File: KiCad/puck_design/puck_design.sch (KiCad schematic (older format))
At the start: 29 parts, among them J1 Coax_Jack, J2 SJ-2523-SMT-TR, Q1 CSD16406Q3, Q2 CSD16406Q3, U1 ITG-3701, U2 BT840F, U3 TE832-M1, U4 MCP73831-2, U5 BQ29700DSER

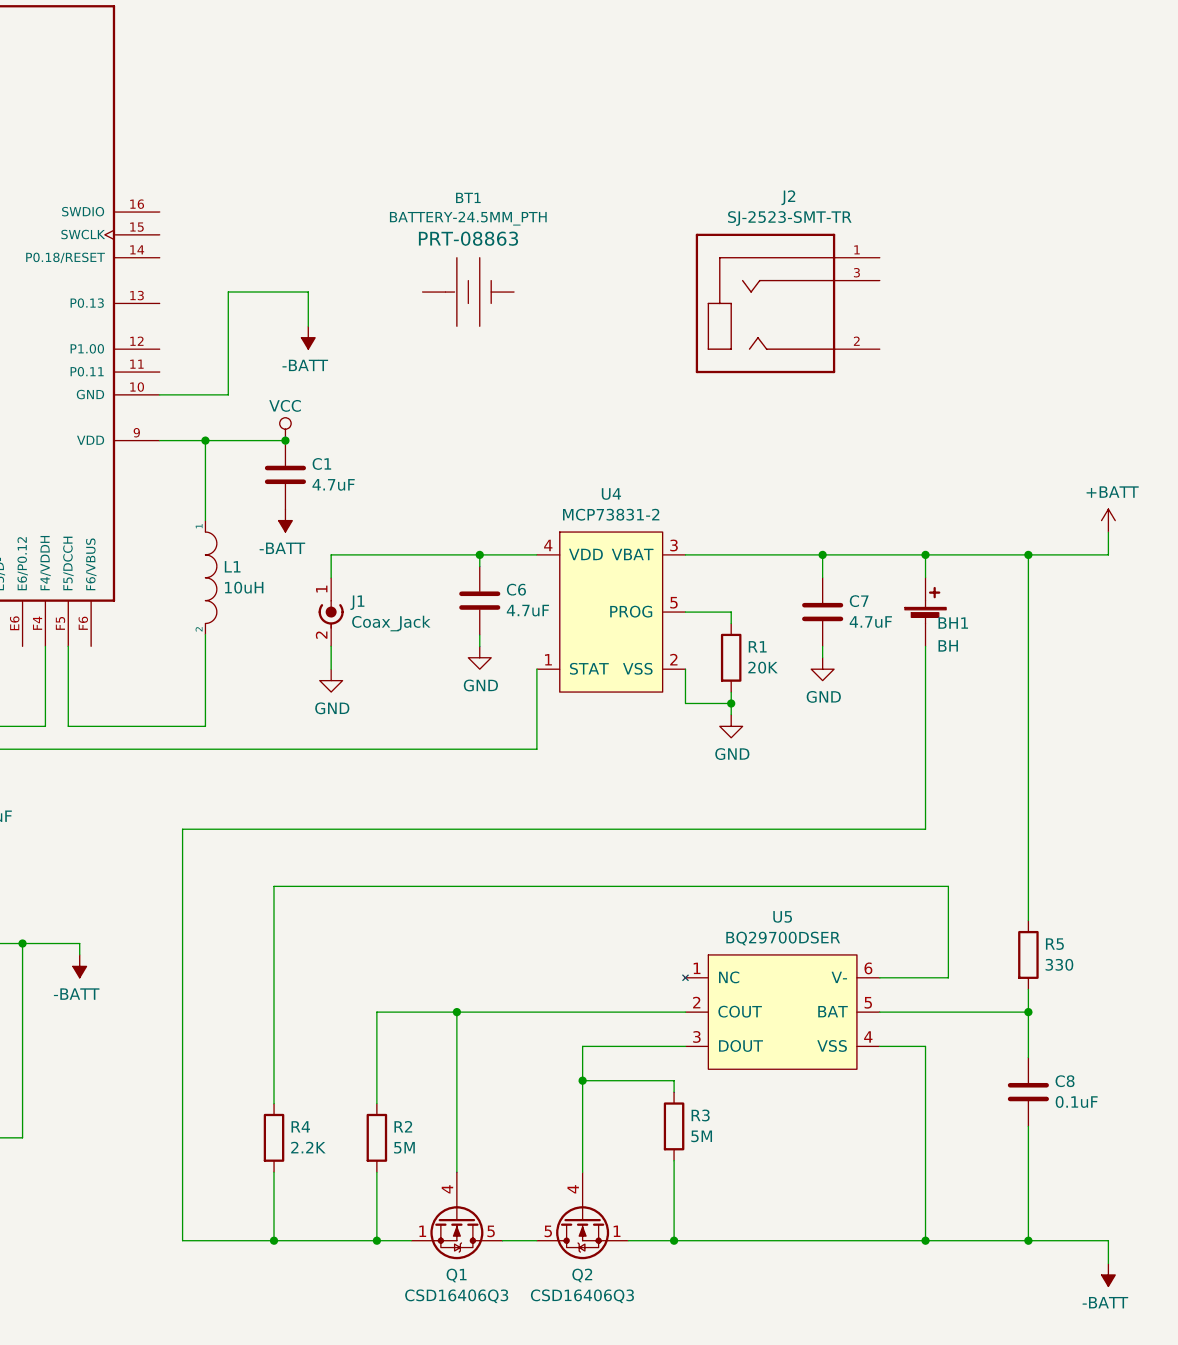
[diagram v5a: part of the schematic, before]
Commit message: Added inductor footprint
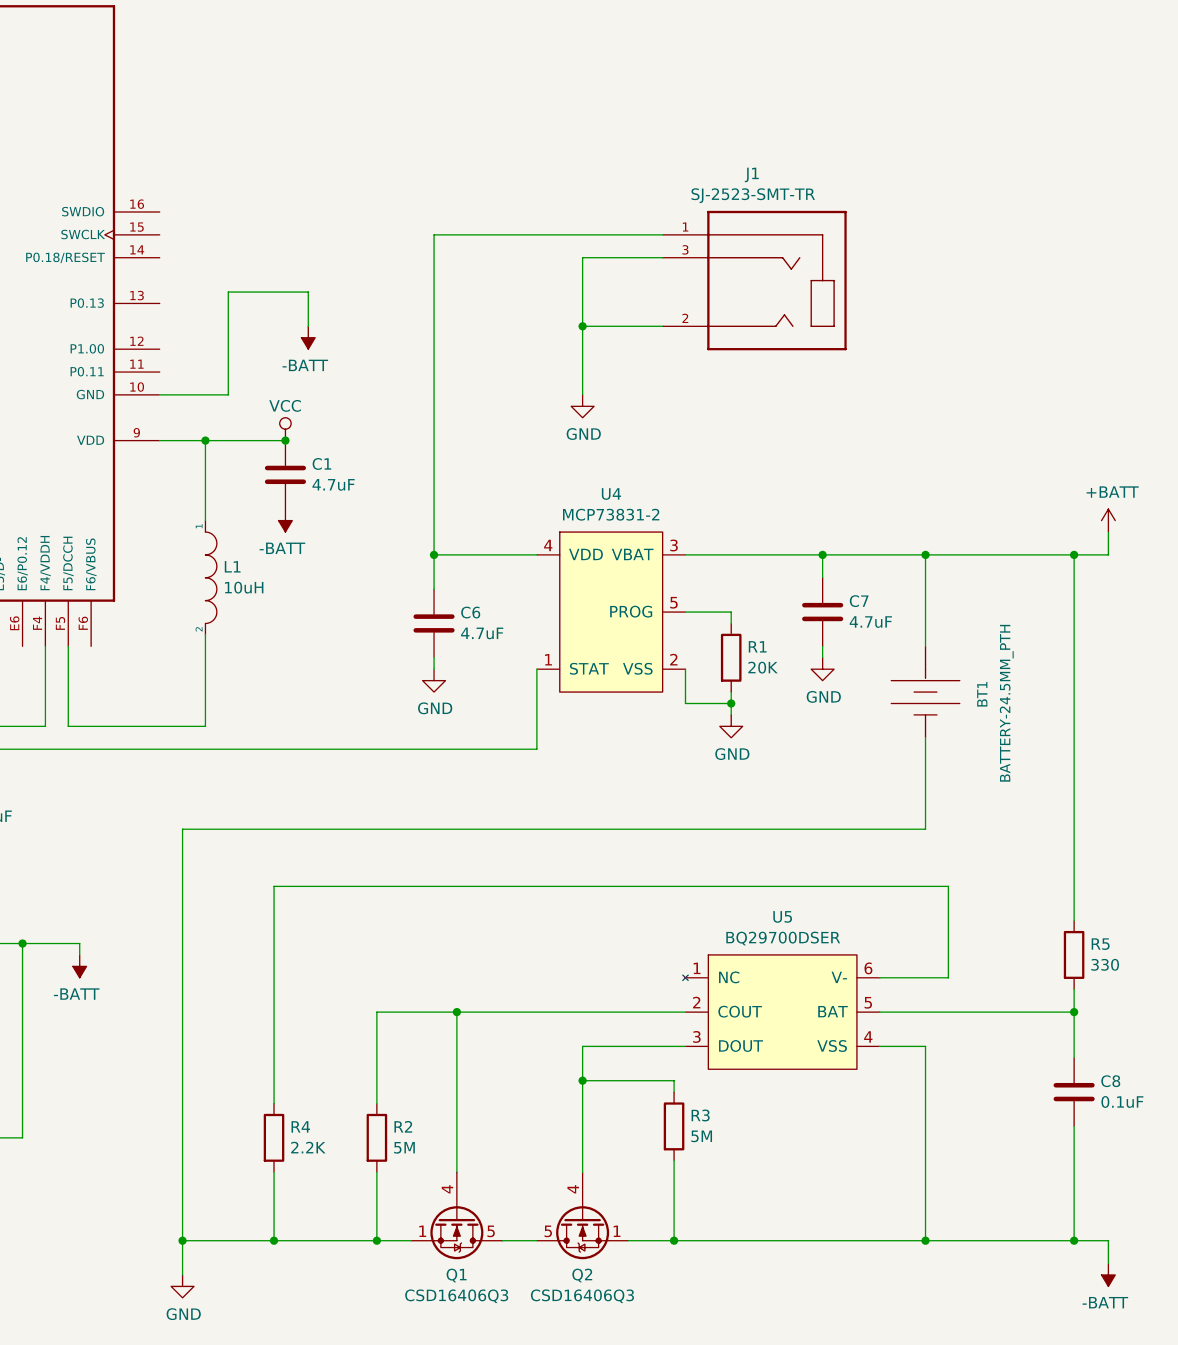
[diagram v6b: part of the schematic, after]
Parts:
- removed BH1: BH, puck_footprints:BATTCON_24.5MM_PTH, symbol Device:Battery_Cell
- removed J1: Coax_Jack, puck_footprints:CUI_SJ-2523-SMT-TR, symbol Connector:Conn_Coaxial_Power
- BT1: Field4 PRT-08863 -> (none)
- L1: footprint (none) -> puck_footprints:CAPC2012X135N
- renumbered J2 to J1
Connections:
- net +BATT: now also BT1.1 (+)
- net GND: now also BT1.2 (-), J1.2, J1.3, Q1.1 (S), Q1.2 (S), Q1.3 (S), R2.2, R4.2
- net at C6.1, U4.4 (VDD): now also J1.1
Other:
- moved on the sheet: C6, C8, J1, R5
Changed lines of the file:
@@
-$EndComp
-$Comp
-L Device:Battery_Cell BH1
-U 1 1 5C20407B
-P 10000 3450
-F 0 "BH1" H 10050 3450 50  0000 L CNN
-F 1 "BH" H 10050 3350 50  0000 L CNN
-F 2 "puck_footprints:BATTCON_24.5MM_PTH" V 10000 3510 50  0001 C CNN
-F 3 "~" V 10000 3510 50  0001 C CNN
-	1    10000 3450
-	1    0    0    -1
 $EndComp
 $Comp
@@
 L power:GND #PWR0115
 U 1 1 5C1E4D3E
-P 7400 3650
-F 0 "#PWR0115" H 7400 3400 50  0001 C CNN
-F 1 "GND" H 7405 3477 50  0000 C CNN
-F 2 "" H 7400 3650 50  0001 C CNN
-F 3 "" H 7400 3650 50  0001 C CNN
-	1    7400 3650
+P 8500 2450
+F 0 "#PWR0115" H 8500 2200 50  0001 C CNN
+F 1 "GND" H 8505 2277 50  0000 C CNN
+F 2 "" H 8500 2450 50  0001 C CNN
+F 3 "" H 8500 2450 50  0001 C CNN
+	1    8500 2450
 	1    0    0    -1
 $EndComp
@@
 L Device:C C6
 U 1 1 5C1C0D7E
-P 8050 3350
-F 0 "C6" H 8165 3396 50  0000 L CNN
-F 1 "4.7uF" H 8165 3305 50  0000 L CNN
-F 2 "puck_footprints:CAPC2012X140N" H 8088 3200 50  0001 C CNN
-F 3 "~" H 8050 3350 50  0001 C CNN
-	1    8050 3350
+P 7850 3450
+F 0 "C6" H 7965 3496 50  0000 L CNN
+F 1 "4.7uF" H 7965 3405 50  0000 L CNN
+F 2 "puck_footprints:CAPC2012X140N" H 7888 3300 50  0001 C CNN
+F 3 "~" H 7850 3450 50  0001 C CNN
+	1    7850 3450
 	1    0    0    -1
 $EndComp
@@
 L power:GND #PWR0119
 U 1 1 5C1CC93A
-P 8050 3550
-F 0 "#PWR0119" H 8050 3300 50  0001 C CNN
-F 1 "GND" H 8055 3377 50  0000 C CNN
-F 2 "" H 8050 3550 50  0001 C CNN
-F 3 "" H 8050 3550 50  0001 C CNN
-	1    8050 3550
+P 7850 3650
+F 0 "#PWR0119" H 7850 3400 50  0001 C CNN
+F 1 "GND" H 7855 3477 50  0000 C CNN
+F 2 "" H 7850 3650 50  0001 C CNN
+F 3 "" H 7850 3650 50  0001 C CNN
+	1    7850 3650
 	1    0    0    -1
 $EndComp
@@
 $EndComp
 Wire Wire Line
-	8050 3150 8050 3200
-Connection ~ 8050 3150
-Wire Wire Line
-	8050 3150 8300 3150
-Wire Wire Line
-	8050 3500 8050 3550
+	7850 3600 7850 3650
 Wire Wire Line
 	9550 3550 9550 3600
@@
 	9550 3150 10000 3150
 Connection ~ 9550 3150
-Wire Wire Line
-	10000 3150 10000 3250
 $Comp
 L puck_library:BQ29700DSER U5
@@
 L Device:R R5
 U 1 1 5C3A4125
-P 10450 4900
-F 0 "R5" H 10520 4946 50  0000 L CNN
-F 1 "330" H 10520 4855 50  0000 L CNN
-F 2 "puck_footprints:0805-NO" V 10380 4900 50  0001 C CNN
-F 3 "~" H 10450 4900 50  0001 C CNN
-	1    10450 4900
+P 10650 4900
+F 0 "R5" H 10720 4946 50  0000 L CNN
+F 1 "330" H 10720 4855 50  0000 L CNN
+F 2 "puck_footprints:0805-NO" V 10580 4900 50  0001 C CNN
+F 3 "~" H 10650 4900 50  0001 C CNN
+	1    10650 4900
 	1    0    0    -1
 $EndComp
@@
 L Device:C C8
 U 1 1 5C3A412C
-P 10450 5500
-F 0 "C8" H 10565 5546 50  0000 L CNN
-F 1 "0.1uF" H 10565 5455 50  0000 L CNN
-F 2 "puck_footprints:CAPC2012X140N" H 10488 5350 50  0001 C CNN
-F 3 "~" H 10450 5500 50  0001 C CNN
-	1    10450 5500
-	1    0    0    -1
-$EndComp
-Wire Wire Line
-	10450 5650 10450 6150
-Wire Wire Line
-	10450 5050 10450 5150
-Wire Wire Line
-	9800 5150 10450 5150
-Connection ~ 10450 5150
-Wire Wire Line
-	10450 5150 10450 5350
+P 10650 5500
+F 0 "C8" H 10765 5546 50  0000 L CNN
+F 1 "0.1uF" H 10765 5455 50  0000 L CNN
+F 2 "puck_footprints:CAPC2012X140N" H 10688 5350 50  0001 C CNN
+F 3 "~" H 10650 5500 50  0001 C CNN
+	1    10650 5500
+	1    0    0    -1
+$EndComp
+Wire Wire Line
+	10650 5650 10650 6150
+Wire Wire Line
+	10650 5050 10650 5150
+Connection ~ 10650 5150
+Wire Wire Line
+	10650 5150 10650 5350
 Wire Wire Line
 	8900 6150 10000 6150
@@
 Connection ~ 10000 6150
 Wire Wire Line
-	10000 6150 10450 6150
-Wire Wire Line
-	10000 3150 10450 3150
-Wire Wire Line
-	10450 3150 10450 4750
+	10650 3150 10650 4750
 Connection ~ 10000 3150
 Wire Wire Line
@@
 	6750 6150 7150 6150
 Wire Wire Line
-	10000 4350 10000 3550
-Wire Wire Line
 	6750 4350 10000 4350
-$Comp
-L Connector:Conn_Coaxial_Power J1
-U 1 1 5C43F4A5
-P 7400 3350
-F 0 "J1" H 7488 3346 50  0000 L CNN
-F 1 "Coax_Jack" H 7488 3255 50  0000 L CNN
-F 2 "puck_footprints:CUI_SJ-2523-SMT-TR" H 7400 3300 50  0001 C CNN
-F 3 "~" H 7400 3300 50  0001 C CNN
-	1    7400 3350
-	1    0    0    -1
-$EndComp
-Wire Wire Line
-	7400 3250 7400 3150
-Wire Wire Line
-	7400 3150 8050 3150
-Wire Wire Line
-	7400 3550 7400 3650
 $Comp
 L pspice:INDUCTOR L1
@@
 F 0 "L1" V 6804 3328 50  0000 L CNN
 F 1 "10uH" V 6895 3328 50  0000 L CNN
-F 2 "" H 6850 3250 50  0001 C CNN
+F 2 "puck_footprints:CAPC2012X135N" H 6850 3250 50  0001 C CNN
 F 3 "~" H 6850 3250 50  0001 C CNN
 	1    6850 3250
@@
 Wire Wire Line
 	6850 2650 7200 2650
-Connection ~ 10450 6150
 $Comp
 L power:-BATT #PWR0101
@@
 Wire Wire Line
 	10800 6150 10800 6250
-Wire Wire Line
-	10450 6150 10800 6150
 $Comp
 L power:+BATT #PWR0102
@@
 $EndComp
 Wire Wire Line
-	10450 3150 10800 3150
-Wire Wire Line
 	10800 3150 10800 3050
-Connection ~ 10450 3150
 $Comp
 L power:+BATT #PWR0103
@@
 	6850 3500 6850 3900
 $Comp
-L puck_library:BATTERY-24.5MM_PTH BT1
-U 1 1 5C3705F2
-P 8000 2000
-F 0 "BT1" H 8000 2410 45  0000 C CNN
-F 1 "BATTERY-24.5MM_PTH" H 8000 2326 45  0000 C CNN
-F 2 "puck_footprints:BATTCON_24.5MM_PTH" H 8000 2250 20  0001 C CNN
-F 3 "" H 8000 2000 50  0001 C CNN
-F 4 "PRT-08863" H 8000 2231 60  0000 C CNN "Field4"
-	1    8000 2000
-	1    0    0    -1
-$EndComp
-$Comp
-L puck_library:SJ-2523-SMT-TR J2
+L puck_library:SJ-2523-SMT-TR J1
 U 1 1 5C370698
-P 9300 2050
-F 0 "J2" H 9405 2517 50  0000 C CNN
-F 1 "SJ-2523-SMT-TR" H 9405 2426 50  0000 C CNN
-F 2 "puck_footprints:CUI_SJ-2523-SMT-TR" H 9300 2050 50  0001 L BNN
-F 3 "SJ-2523-SMT-TR" H 9300 2050 50  0001 L BNN
-F 4 "None" H 9300 2050 50  0001 L BNN "Field4"
-F 5 "CUI Inc." H 9300 2050 50  0001 L BNN "Field5"
-F 6 "https://www.cui.com/product/interconnect/audio-connectors/jacks/2.5-mm-jacks/sj-252x-smt-series?utm_source=snapeda.com&utm_medium=referral&utm_campaign=snapedaBOM" H 7100 2600 50  0001 L BNN "Field6"
-F 7 "https://www.digikey.com/product-detail/en/cui-inc/SJ-2523-SMT-TR/CP-2523SJCT-ND/669702?utm_source=snapeda&utm_medium=aggregator&utm_campaign=symbol" H 7100 2600 50  0001 L BNN "Field7"
-F 8 "SJ Series 2.5 mm SMT Right Angle Stereo Audio Jack" H 7100 2600 50  0001 L BNN "Field8"
-F 9 "CP-2523SJCT-ND" H 9300 2050 50  0001 L BNN "Field9"
-	1    9300 2050
-	1    0    0    -1
+P 9350 1950
+F 0 "J1" H 9455 2417 50  0000 C CNN
+F 1 "SJ-2523-SMT-TR" H 9455 2326 50  0000 C CNN
+F 2 "puck_footprints:CUI_SJ-2523-SMT-TR" H 9350 1950 50  0001 L BNN
+F 3 "SJ-2523-SMT-TR" H 9350 1950 50  0001 L BNN
+F 4 "None" H 9350 1950 50  0001 L BNN "Field4"
+F 5 "CUI Inc." H 9350 1950 50  0001 L BNN "Field5"
+F 6 "https://www.cui.com/product/interconnect/audio-connectors/jacks/2.5-mm-jacks/sj-252x-smt-series?utm_source=snapeda.com&utm_medium=referral&utm_campaign=snapedaBOM" H 7150 2500 50  0001 L BNN "Field6"
+F 7 "https://www.digikey.com/product-detail/en/cui-inc/SJ-2523-SMT-TR/CP-2523SJCT-ND/669702?utm_source=snapeda&utm_medium=aggregator&utm_campaign=symbol" H 7150 2500 50  0001 L BNN "Field7"
+F 8 "SJ Series 2.5 mm SMT Right Angle Stereo Audio Jack" H 7150 2500 50  0001 L BNN "Field8"
+F 9 "CP-2523SJCT-ND" H 9350 1950 50  0001 L BNN "Field9"
+	1    9350 1950
+	-1   0    0    -1
 $EndComp
 Wire Wire Line
@@
 Wire Wire Line
 	5350 4000 8300 4000
+$Comp
+L puck_library:BATTERY-24.5MM_PTH BT1
+U 1 1 5C388373
+P 10000 3750
+F 0 "BT1" H 9950 4000 45  0000 L CNN
+F 1 "BATTERY-24.5MM_PTH" H 9700 4100 45  0000 L CNN
+F 2 "puck_footprints:BATTCON_24.5MM_PTH" H 9950 4050 20  0001 C CNN
+F 3 "" H 10000 3750 50  0001 C CNN
+	1    10000 3750
+	0    1    1    0
+$EndComp
+Wire Wire Line
+	10000 3150 10000 3550
+Wire Wire Line
+	10000 4350 10000 3950
+Wire Wire Line
+	8850 2150 8500 2150
+Wire Wire Line
+	8500 2150 8500 2450
+Wire Wire Line
+	8850 1850 8500 1850
+Wire Wire Line
+	8500 1850 8500 2150
+Connection ~ 8500 2150
+Wire Wire Line
+	7850 1750 7850 3150
+Wire Wire Line
+	7850 1750 8850 1750
+Wire Wire Line
+	7850 3150 7850 3300
+Wire Wire Line
+	7850 3150 8300 3150
+Connection ~ 7850 3150
+Connection ~ 10650 3150
+Wire Wire Line
+	10650 3150 10800 3150
+Connection ~ 10650 6150
+Wire Wire Line
+	10650 6150 10800 6150
+Wire Wire Line
+	10000 6150 10650 6150
+Wire Wire Line
+	10000 3150 10650 3150
+Wire Wire Line
+	9800 5150 10650 5150
+$Comp
+L power:GND #PWR0125
+U 1 1 5C40E50A
+P 6750 6300
+F 0 "#PWR0125" H 6750 6050 50  0001 C CNN
+F 1 "GND" H 6755 6127 50  0000 C CNN
+F 2 "" H 6750 6300 50  0001 C CNN
+F 3 "" H 6750 6300 50  0001 C CNN
+	1    6750 6300
+	1    0    0    -1
+$EndComp
+Wire Wire Line
+	6750 6300 6750 6150
+Connection ~ 6750 6150
 $EndSCHEMATC

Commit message: Updated schematic and added PCB layout with gerber/drill files
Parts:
- removed Q1, Q2: CSD16406Q3, puck_footprints:CSD16406Q3, symbol Transistor_FET:CSD16408Q5
- added D1: Debug, puck_footprints:Debug Header, symbol puck_library:Debug
- added Q1, Q2: CSD16406Q3, puck_footprints:CSD16406Q3, symbol puck_library:CSD16406Q3
- U4: value MCP73831-2 -> MCP73832-2; footprint puck_footprints:MCP73831T_2ATI_OT -> puck_footprints:MCP73832T_2ATI_OT
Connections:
- net -BATT is gone; now on net GND: C1.2, C2.2, C3.2, C4.2, C5.2, C8.2, C9.2, CX1.2, CX2.2, CX3.2, R3.2, U1.12 (GND), U1.14 (RESV-G), U1.8 (FSYNC), U2.10 (GND), U2.A0 (A0/VSS1), U2.B0 (B0/VSS2), U2.C0 (C0/VSS3), U2.D0 (D0/VSS4), U2.F0 (F0/GND), U2.F1 (F1/GND), U2.F2 (F2/GND), U2.F3 (F3/GND), U3.3 (GND), U5.4 (VSS)
- net GND: now also J1.1, D1.4 (GND), Q1.1 (S), Q1.2 (S), Q1.3 (S), Q2.1 (S), Q2.2 (S), Q2.3 (S); no longer J1.2, J1.3
- net VCC: now also D1.3 (VDD)
- net at U1.1 (SDA/SDI): now also U2.C6 (C6/P1.04); no longer U2.B5 (B5/P0.08)
- net at U1.10 (INT): now also U2.D6 (D6/P105)
- net at U1.16 (SCL/SCLK): now also U2.D5 (D5/P0.11); no longer U2.C4 (C4/P0.15)
- net at U1.4 (/CS): now also U2.B6 (B6/P1.03); no longer U2.B1 (B1/P0.25)
- net at U1.6 (AD0/SDO): now also U2.A6 (A6/P1.08); no longer U2.B3 (B3/P0.31)
- net at CX3.1, U3.4 (+Z): now also U2.A4 (A4/P0.05); no longer U2.A2 (A2/P0.29)
- net at U2.15 (SWCLK): now also D1.2 (SWCLK)
- net at U2.16 (SWDIO): now also D1.1 (SWDIO)
- net at U4.1 (STAT): now also U2.E6 (E6/P0.12); no longer U2.D6 (D6/P105)
- net at C6.1, U4.4 (VDD): now also J1.2, J1.3; no longer J1.1
- net at R2.1, U5.2 (COUT): now also Q1.4 (G)
- net at R3.1, U5.3 (DOUT): now also Q2.4 (G)
- new net: Q1.9 (D), Q2.9 (D)
- no-connect marks 0 -> 49
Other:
- moved on the sheet: BT1, C6, J1
